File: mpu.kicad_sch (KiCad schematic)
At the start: 166 parts, among them J1 USB_OTG, J2 DIN41612_02x10_AB, J3 USB_OTG, J4 Conn_02x20_Counter_Clockwise, J5 Conn_01x15_Socket, U3 ECMF02-2AMX6, U4 ECMF02-2AMX6, U5 STM32MP157FADx, X1 ASE-24MHz

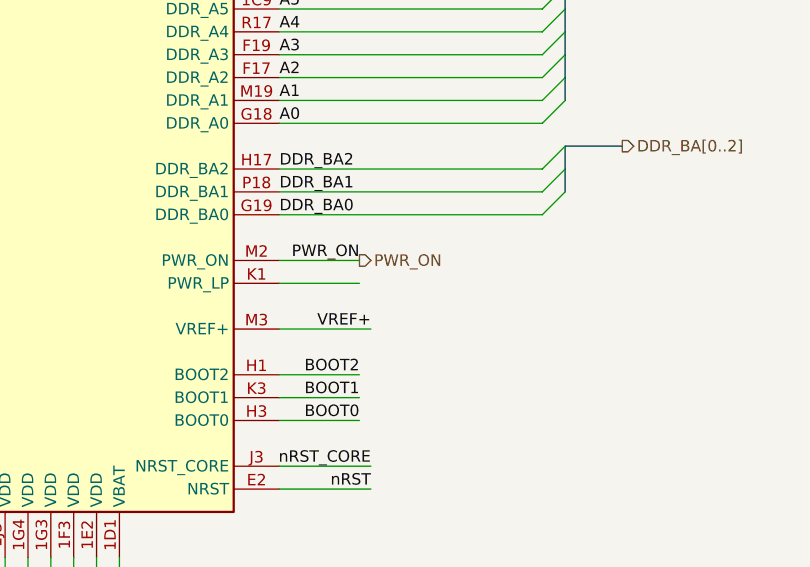
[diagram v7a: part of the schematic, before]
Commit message: Finished routing and added LP_PWR connection
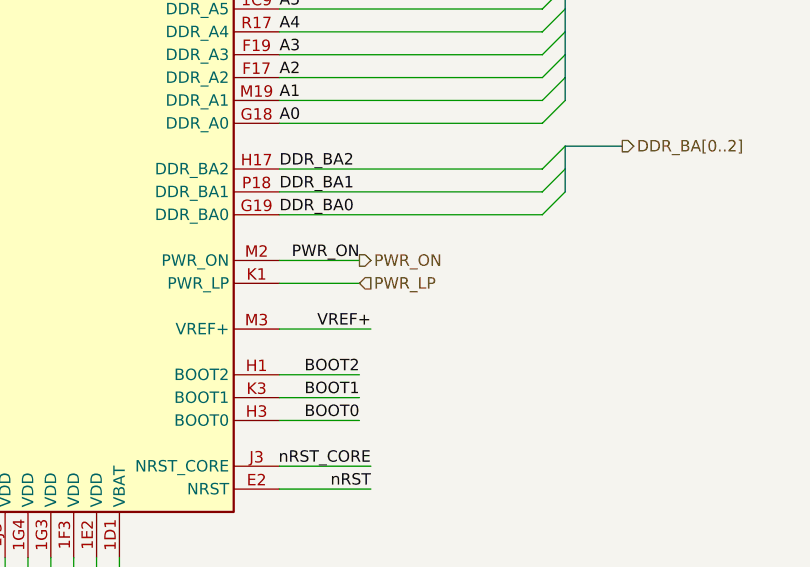
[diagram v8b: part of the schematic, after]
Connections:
- net PWR_LP: now reaches U5.K1 (PWR_LP)
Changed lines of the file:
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@@
+		)
+	)
+	(hierarchical_label "PWR_LP"
+		(shape input)
+		(at 205.74 285.75 0)
+		(fields_autoplaced yes)
+		(effects
+			(font
+				(size 1.27 1.27)
+			)
+			(justify left)
 		)
 	)
@@
 			(justify left)
 		)
-		(property "Target_Skew" "1.0mm"
-			(at 234.95 228.6 0)
-			(effects
-				(font
-					(size 1.27 1.27)
-					(italic yes)
-				)
-				(justify left)
-				(hide yes)
-			)
-		)
-	)
+	)
